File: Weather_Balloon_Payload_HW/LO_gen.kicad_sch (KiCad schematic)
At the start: 63 parts, among them J5 MM8430-2610, J6 MM8430-2610, T1 CX2045LNLT, U10 PGA-105, U11 PGA-105, U12 TLV9061, U13 MAX2608, U14 TS5A3159ADBVR, U9 ADF4002BRUZ

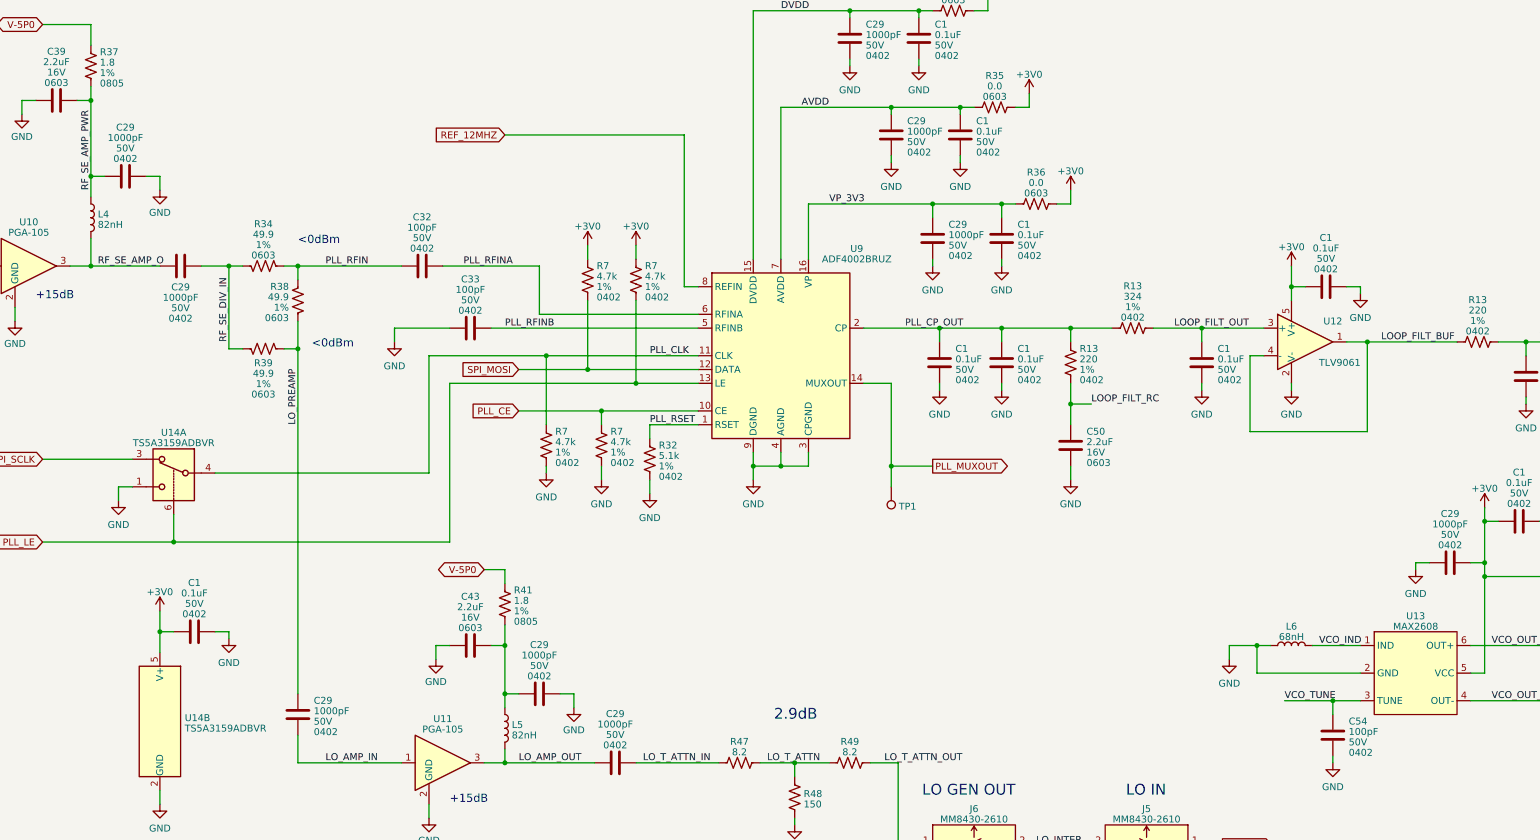
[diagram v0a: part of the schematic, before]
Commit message: Update README, block diagrams, schem. Begin layout
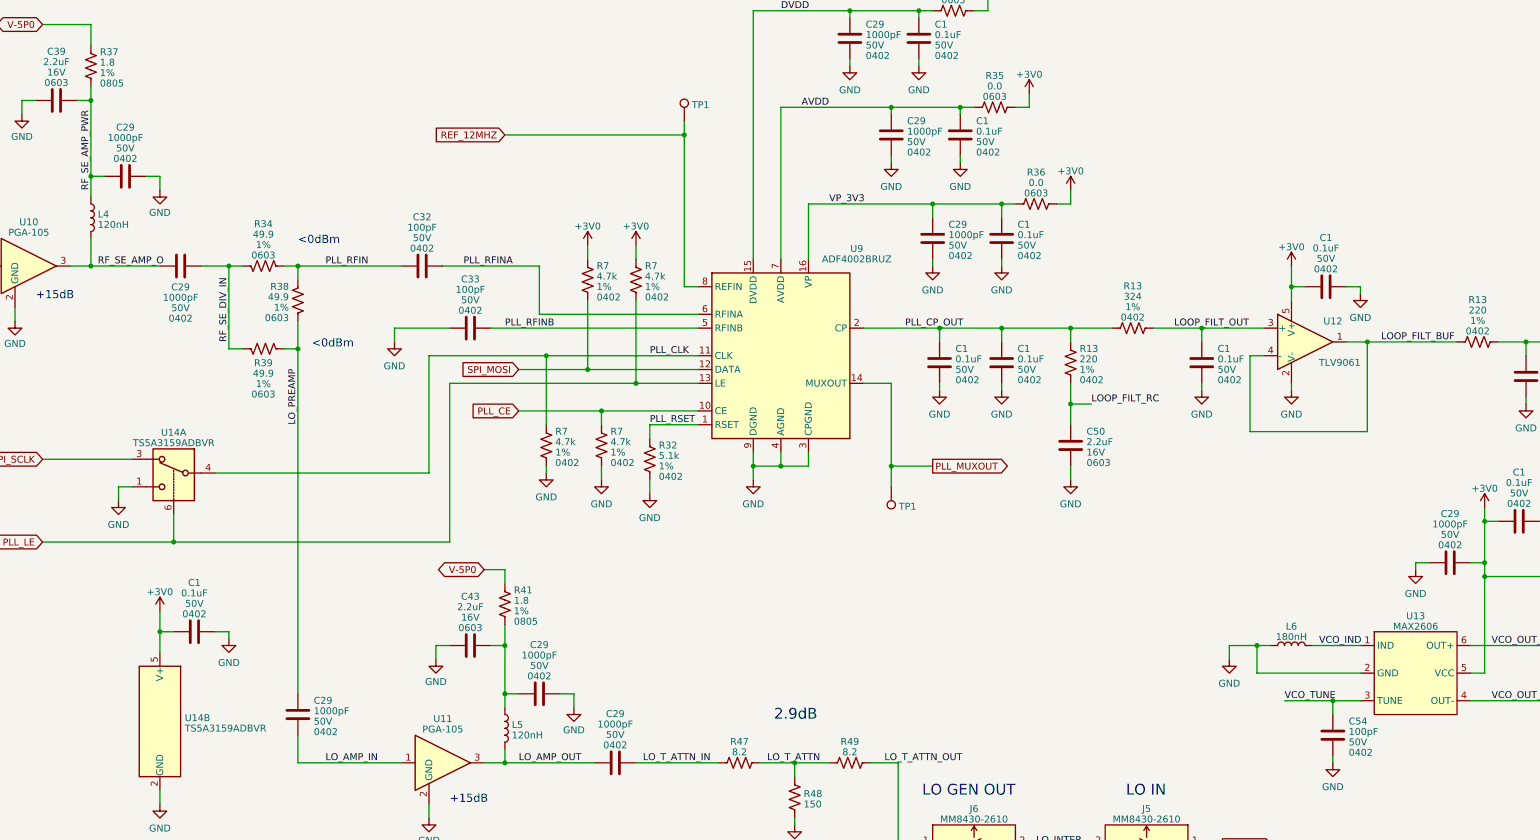
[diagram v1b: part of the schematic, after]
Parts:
- added TP1: TestPoint, TestPoint:TestPoint_Pad_D1.0mm, symbol Connector:TestPoint
- L4, L5: value 82nH -> 120nH; footprint Inductor_SMD:L_1008_2520Metric -> Inductor_SMD:L_1008_2520Metric_Pad1.43x2.20mm_HandSolder; JLCPCB Part # C703708 -> C703706; Mfr. Part # LQW2UAS82NG00L -> LQW2UASR12G00L
- L6: value 68nH -> 180nH; footprint Inductor_SMD:L_1008_2520Metric -> Inductor_SMD:L_0805_2012Metric_Pad1.15x1.40mm_HandSolder; Mfr. Part # 1008CS-680XJLC -> 0805HP-181XJRC
- U13: value MAX2608 -> MAX2606; MFG_PN MAX2608EUT+T -> MAX2606EUT+T
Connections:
- net REF_12MHZ: now also TP1.1
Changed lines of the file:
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@@
   (junction (at 236.22 128.27) (diameter 0) (color 0 0 0 0)
   )
+  (junction (at 177.8 92.71) (diameter 0) (color 0 0 0 0)
+  )
   (junction (at 325.12 171.45) (diameter 0) (color 0 0 0 0)
   )
@@
     (stroke (width 0) (type default))
   )
+  (wire (pts (xy 177.8 90.17) (xy 177.8 92.71))
+    (stroke (width 0) (type default))
+  )
   (wire (pts (xy 289.56 120.65) (xy 292.1 120.65))
     (stroke (width 0) (type default))
@@
     )
   )
+  (symbol (lib_id "Device:L") (at 144.78 201.93 0) (unit 1)
+    (in_bom yes) (on_board yes) (dnp no) (fields_autoplaced)
+    (property "Reference" "L5" (at 146.0472 201.2863 0)
+      (effects (font (size 1.27 1.27)) (justify left))
+    )
+    (property "Value" "120nH" (at 146.0472 203.2073 0)
+      (effects (font (size 1.27 1.27)) (justify left))
+    )
+    (property "Footprint" "Inductor_SMD:L_1008_2520Metric_Pad1.43x2.20mm_HandSolder" (at 144.78 201.93 0)
+      (effects (font (size 1.27 1.27)) hide)
+    )
+    (property "Datasheet" "~" (at 144.78 201.93 0)
+      (effects (font (size 1.27 1.27)) hide)
+    )
+    (property "Mfr. Part #" "LQW2UASR12G00L" (at 144.78 201.93 0)
+      (effects (font (size 1.27 1.27)) hide)
+    )
+    (property "JLCPCB Part #" "C703706" (at 144.78 201.93 0)
+      (effects (font (size 1.27 1.27)) hide)
+    )
+    (pin "1")
+    (pin "2")
+    (instances
+      (project "Weather_Balloon_Payload_HW"
+        (path "/5c4ed951-5674-406c-8bab-ae3e3237b79b/d25c89f3-6f65-404d-b20b-3f5c88d9a813"
+          (reference "L5") (unit 1)
+        )
+        (path "/5c4ed951-5674-406c-8bab-ae3e3237b79b/7518f41b-5c0d-4c59-b494-678674f8b2a3"
+          (reference "L11") (unit 1)
+        )
+      )
+      (project "FM_Radio_70cm_HW"
+        (path "/dd3ca0f2-57ae-4d6e-a47c-2bc06831656e/f97f3696-4068-4315-ad42-990afe512e35"
+          (reference "L11") (unit 1)
+        )
+        (path "/dd3ca0f2-57ae-4d6e-a47c-2bc06831656e/5d1d0483-5da8-47ba-a805-030f4b7f5b2d"
+          (reference "L15") (unit 1)
+        )
+      )
+    )
+  )
   (symbol (lib_id "power:GND") (at 337.82 165.1 0) (unit 1)
     (in_bom yes) (on_board yes) (dnp no) (fields_autoplaced)
@@
       (effects (font (size 1.27 1.27)))
     )
-    (property "Value" "MAX2608" (at 312.42 183.1881 0)
+    (property "Value" "MAX2606" (at 312.42 183.1881 0)
       (effects (font (size 1.27 1.27)))
     )
@@
       (effects (font (size 1.27 1.27)) hide)
     )
-    (property "MFG_PN" "MAX2608EUT+T" (at 312.42 184.15 0)
+    (property "MFG_PN" "MAX2606EUT+T" (at 312.42 184.15 0)
       (effects (font (size 1.27 1.27)) hide)
     )
@@
       (effects (font (size 1.27 1.27)))
     )
-    (property "Value" "68nH" (at 289.56 185.0957 90)
+    (property "Value" "180nH" (at 289.56 185.0957 90)
       (effects (font (size 1.27 1.27)))
     )
-    (property "Footprint" "Inductor_SMD:L_1008_2520Metric" (at 289.56 186.69 0)
+    (property "Footprint" "Inductor_SMD:L_0805_2012Metric_Pad1.15x1.40mm_HandSolder" (at 289.56 186.69 0)
       (effects (font (size 1.27 1.27)) hide)
     )
@@
       (effects (font (size 1.27 1.27)) hide)
     )
-    (property "Mfr. Part #" "1008CS-680XJLC" (at 289.56 186.69 90)
+    (property "Mfr. Part #" "0805HP-181XJRC" (at 289.56 186.69 90)
       (effects (font (size 1.27 1.27)) hide)
     )
@@
     )
   )
+  (symbol (lib_id "Device:L") (at 68.58 107.95 0) (unit 1)
+    (in_bom yes) (on_board yes) (dnp no) (fields_autoplaced)
+    (property "Reference" "L4" (at 69.8472 107.3063 0)
+      (effects (font (size 1.27 1.27)) (justify left))
+    )
+    (property "Value" "120nH" (at 69.8472 109.2273 0)
+      (effects (font (size 1.27 1.27)) (justify left))
+    )
+    (property "Footprint" "Inductor_SMD:L_1008_2520Metric_Pad1.43x2.20mm_HandSolder" (at 68.58 107.95 0)
+      (effects (font (size 1.27 1.27)) hide)
+    )
+    (property "Datasheet" "~" (at 68.58 107.95 0)
+      (effects (font (size 1.27 1.27)) hide)
+    )
+    (property "Mfr. Part #" "LQW2UASR12G00L" (at 68.58 107.95 0)
+      (effects (font (size 1.27 1.27)) hide)
+    )
+    (property "JLCPCB Part #" "C703706" (at 68.58 107.95 0)
+      (effects (font (size 1.27 1.27)) hide)
+    )
+    (pin "1")
+    (pin "2")
+    (instances
+      (project "Weather_Balloon_Payload_HW"
+        (path "/5c4ed951-5674-406c-8bab-ae3e3237b79b/d25c89f3-6f65-404d-b20b-3f5c88d9a813"
+          (reference "L4") (unit 1)
+        )
+        (path "/5c4ed951-5674-406c-8bab-ae3e3237b79b/7518f41b-5c0d-4c59-b494-678674f8b2a3"
+          (reference "L11") (unit 1)
+        )
+      )
+      (project "FM_Radio_70cm_HW"
+        (path "/dd3ca0f2-57ae-4d6e-a47c-2bc06831656e/f97f3696-4068-4315-ad42-990afe512e35"
+          (reference "L11") (unit 1)
+        )
+        (path "/dd3ca0f2-57ae-4d6e-a47c-2bc06831656e/5d1d0483-5da8-47ba-a805-030f4b7f5b2d"
+          (reference "L15") (unit 1)
+        )
+      )
+    )
+  )
   (symbol (lib_id "Device:R_US") (at 337.82 180.34 0) (unit 1)
     (in_bom yes) (on_board yes) (dnp no) (fields_autoplaced)
@@
     )
   )
+  (symbol (lib_id "Connector:TestPoint") (at 177.8 90.17 0) (unit 1)
+    (in_bom yes) (on_board yes) (dnp no) (fields_autoplaced)
+    (property "Reference" "TP1" (at 179.197 87.1848 0)
+      (effects (font (size 1.27 1.27)) (justify left))
+    )
+    (property "Value" "TestPoint" (at 179.0773 85.471 90)
+      (effects (font (size 1.27 1.27)) (justify left) hide)
+    )
+    (property "Footprint" "TestPoint:TestPoint_Pad_D1.0mm" (at 182.88 90.17 0)
+      (effects (font (size 1.27 1.27)) hide)
+    )
+    (property "Datasheet" "~" (at 182.88 90.17 0)
+      (effects (font (size 1.27 1.27)) hide)
+    )
+    (pin "1")
+    (instances
+      (project "Weather_Balloon_Payload_HW"
+        (path "/5c4ed951-5674-406c-8bab-ae3e3237b79b/5c1aaf52-29f1-4510-8945-25db72c84267"
+          (reference "TP1") (unit 1)
+        )
+        (path "/5c4ed951-5674-406c-8bab-ae3e3237b79b/f83fd516-1a4d-4b5e-9499-2c791d3fffe0"
+          (reference "TP5") (unit 1)
+        )
+        (path "/5c4ed951-5674-406c-8bab-ae3e3237b79b/d25c89f3-6f65-404d-b20b-3f5c88d9a813"
+          (reference "TP9") (unit 1)
+        )
+      )
+    )
+  )
   (symbol (lib_id "power:GND") (at 152.4 154.94 0) (unit 1)
     (in_bom yes) (on_board yes) (dnp no) (fields_autoplaced)
@@
     )
   )
-  (symbol (lib_id "Device:L") (at 68.58 107.95 0) (unit 1)
-    (in_bom yes) (on_board yes) (dnp no) (fields_autoplaced)
-    (property "Reference" "L4" (at 69.8472 107.3063 0)
-      (effects (font (size 1.27 1.27)) (justify left))
-    )
-    (property "Value" "82nH" (at 69.8472 109.2273 0)
-      (effects (font (size 1.27 1.27)) (justify left))
-    )
-    (property "Footprint" "Inductor_SMD:L_1008_2520Metric" (at 68.58 107.95 0)
-      (effects (font (size 1.27 1.27)) hide)
-    )
-    (property "Datasheet" "~" (at 68.58 107.95 0)
-      (effects (font (size 1.27 1.27)) hide)
-    )
-    (property "Mfr. Part #" "LQW2UAS82NG00L" (at 68.58 107.95 0)
-      (effects (font (size 1.27 1.27)) hide)
-    )
-    (property "JLCPCB Part #" "C703708" (at 68.58 107.95 0)
-      (effects (font (size 1.27 1.27)) hide)
-    )
-    (pin "1")
-    (pin "2")
-    (instances
-      (project "Weather_Balloon_Payload_HW"
-        (path "/5c4ed951-5674-406c-8bab-ae3e3237b79b/d25c89f3-6f65-404d-b20b-3f5c88d9a813"
-          (reference "L4") (unit 1)
-        )
-      )
-      (project "FM_Radio_70cm_HW"
-        (path "/dd3ca0f2-57ae-4d6e-a47c-2bc06831656e/f97f3696-4068-4315-ad42-990afe512e35"
-          (reference "L11") (unit 1)
-        )
-        (path "/dd3ca0f2-57ae-4d6e-a47c-2bc06831656e/5d1d0483-5da8-47ba-a805-030f4b7f5b2d"
-          (reference "L14") (unit 1)
-        )
-      )
-    )
-  )
   (symbol (lib_id "Amplifier_Operational:AD8603") (at 292.1 130.81 0) (unit 1)
     (in_bom yes) (on_board yes) (dnp no)
@@
         )
       )
-    )
-  )
-  (symbol (lib_id "Device:L") (at 144.78 201.93 0) (unit 1)
-    (in_bom yes) (on_board yes) (dnp no) (fields_autoplaced)
-    (property "Reference" "L5" (at 146.0472 201.2863 0)
-      (effects (font (size 1.27 1.27)) (justify left))
-    )
-    (property "Value" "82nH" (at 146.0472 203.2073 0)
-      (effects (font (size 1.27 1.27)) (justify left))
-    )
-    (property "Footprint" "Inductor_SMD:L_1008_2520Metric" (at 144.78 201.93 0)
-      (effects (font (size 1.27 1.27)) hide)
-    )
-    (property "Datasheet" "~" (at 144.78 201.93 0)
-      (effects (font (size 1.27 1.27)) hide)
-    )
-    (property "Mfr. Part #" "LQW2UAS82NG00L" (at 144.78 201.93 0)
-      (effects (font (size 1.27 1.27)) hide)
-    )
-    (property "JLCPCB Part #" "C703708" (at 144.78 201.93 0)
-      (effects (font (size 1.27 1.27)) hide)
-    )
-    (pin "1")
-    (pin "2")
-    (instances
-      (project "Weather_Balloon_Payload_HW"
-        (path "/5c4ed951-5674-406c-8bab-ae3e3237b79b/d25c89f3-6f65-404d-b20b-3f5c88d9a813"
-          (reference "L5") (unit 1)
-        )
-      )
-      (project "FM_Radio_70cm_HW"
-        (path "/dd3ca0f2-57ae-4d6e-a47c-2bc06831656e/f97f3696-4068-4315-ad42-990afe512e35"
-          (reference "L11") (unit 1)
-        )
-        (path "/dd3ca0f2-57ae-4d6e-a47c-2bc06831656e/5d1d0483-5da8-47ba-a805-030f4b7f5b2d"
-          (reference "L15") (unit 1)
-        )
-      )

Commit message: Add fabrication files
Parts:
- R13: JLCPCB Part # (none) -> C102889; Manufacturer (none) -> RALEC; Mfr. Part # (none) -> RTT022200FTH
- R13: JLCPCB Part # (none) -> C423191; Manufacturer (none) -> UNI-ROYAL(Uniroyal Elec); Mfr. Part # (none) -> 0402WGF3240TCE
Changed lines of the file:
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@@
       (effects (font (size 1.27 1.27)) hide)
     )
-    (property "Description" "~" (at 323.85 130.81 0)
+    (property "Description" "62.5mW Thick Film Resistors ±100ppm/℃ ±1% 220Ω 0402 Chip" (at 323.85 130.81 0)
       (effects (font (size 1.27 1.27)) hide)
     )
-    (property "JLCPCB Part #" "~" (at 323.85 130.81 0)
+    (property "JLCPCB Part #" "C102889" (at 323.85 130.81 0)
       (effects (font (size 1.27 1.27)) hide)
     )
-    (property "Manufacturer" "~" (at 323.85 130.81 0)
+    (property "Manufacturer" "RALEC" (at 323.85 130.81 0)
       (effects (font (size 1.27 1.27)) hide)
     )
-    (property "Mfr. Part #" "~" (at 323.85 130.81 0)
+    (property "Mfr. Part #" "RTT022200FTH" (at 323.85 130.81 0)
       (effects (font (size 1.27 1.27)) hide)
     )
@@
       (effects (font (size 1.27 1.27)) hide)
     )
-    (property "Description" "~" (at 248.92 134.62 0)
+    (property "Description" "62.5mW Thick Film Resistors ±100ppm/℃ ±1% 220Ω 0402 Chip" (at 248.92 134.62 0)
       (effects (font (size 1.27 1.27)) hide)
     )
-    (property "JLCPCB Part #" "~" (at 248.92 134.62 0)
+    (property "JLCPCB Part #" "C102889" (at 248.92 134.62 0)
       (effects (font (size 1.27 1.27)) hide)
     )
-    (property "Manufacturer" "~" (at 248.92 134.62 0)
+    (property "Manufacturer" "RALEC" (at 248.92 134.62 0)
       (effects (font (size 1.27 1.27)) hide)
     )
-    (property "Mfr. Part #" "~" (at 248.92 134.62 0)
+    (property "Mfr. Part #" "RTT022200FTH" (at 248.92 134.62 0)
       (effects (font (size 1.27 1.27)) hide)
     )
@@
       (effects (font (size 1.27 1.27)) hide)
     )
-    (property "Description" "~" (at 260.35 128.27 0)
+    (property "Description" "62.5mW Thick Film Resistors ±100ppm/℃ ±1% 324Ω 0402 Chip" (at 260.35 128.27 0)
       (effects (font (size 1.27 1.27)) hide)
     )
-    (property "JLCPCB Part #" "~" (at 260.35 128.27 0)
+    (property "JLCPCB Part #" "C423191" (at 260.35 128.27 0)
       (effects (font (size 1.27 1.27)) hide)
     )
-    (property "Manufacturer" "~" (at 260.35 128.27 0)
+    (property "Manufacturer" "UNI-ROYAL(Uniroyal Elec)" (at 260.35 128.27 0)
       (effects (font (size 1.27 1.27)) hide)
     )
-    (property "Mfr. Part #" "~" (at 260.35 128.27 0)
+    (property "Mfr. Part #" "0402WGF3240TCE" (at 260.35 128.27 0)
       (effects (font (size 1.27 1.27)) hide)
     )

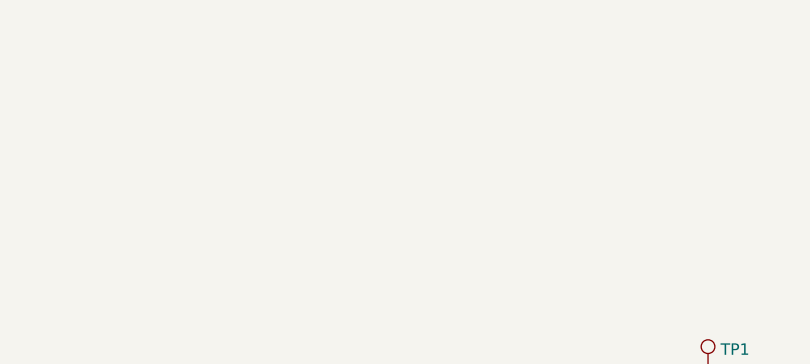
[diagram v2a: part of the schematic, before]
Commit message: Antenna imped match files, boilerplate STM code
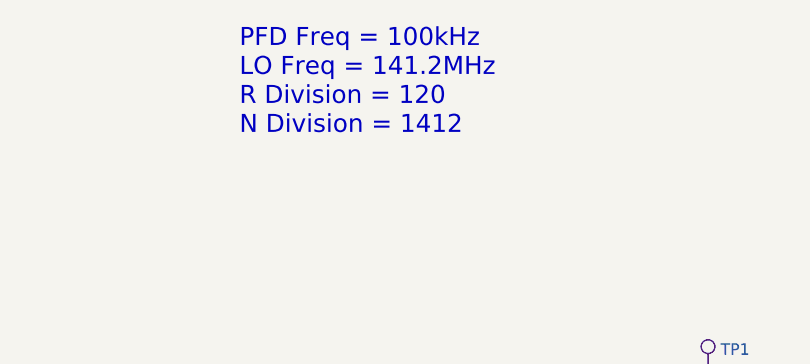
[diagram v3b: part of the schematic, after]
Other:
- note added: "PFD Freq = 100kHz LO Freq = 141.2MHz R Division = 120 N Division = 1412"
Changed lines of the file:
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@@
     (effects (font (size 1.5 1.5)) (justify left bottom))
+  )
+  (text "PFD Freq = 100kHz\nLO Freq = 141.2MHz\nR Division = 120\nN Division = 1412"
+    (at 125.73 63.5 0)
+    (effects (font (size 2 2)) (justify left bottom))
   )
   (text "LO GEN OUT" (at 238.76 214.63 0)
